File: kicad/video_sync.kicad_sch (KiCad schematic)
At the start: 7 parts, among them J17 Monitor Header, U129 74LS221, U130 74LS221

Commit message: update kicad project
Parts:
- added C87, C88: 1000pF, seequa_footprints:C_Seequa_Bypass_6.5mm, symbol Device:C_Small
- added R11, R80: 6.21 kΩ, seequa_footprints:R_Seequa_Resistor, symbol Device:R_Small
- C105: seq_coord (none) -> L36
- C96, J17: seq_coord (none) -> K33
- R44: seq_coord (none) -> L32; seq_silkscreen R40 -> (none)
- R45: seq_coord (none) -> L33
- U129, U130: seq_coord (none) -> K32; seq_silkscreen (none) -> LS221
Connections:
- net +5V: now also R11.2, R80.2
- net at U129.14 (Cext): now also C87.1
- net at U129.15 (RCext): now also C87.2, R80.1
- net at U129.6 (Cext): now also C88.1
- net at U129.7 (RCext): now also C88.2, R11.1
- net HSYNC_END renamed FRONT_PORCH
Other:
- note added: "Composite HSYNC Pulse"
- note added: "Composite front porch / color burst"

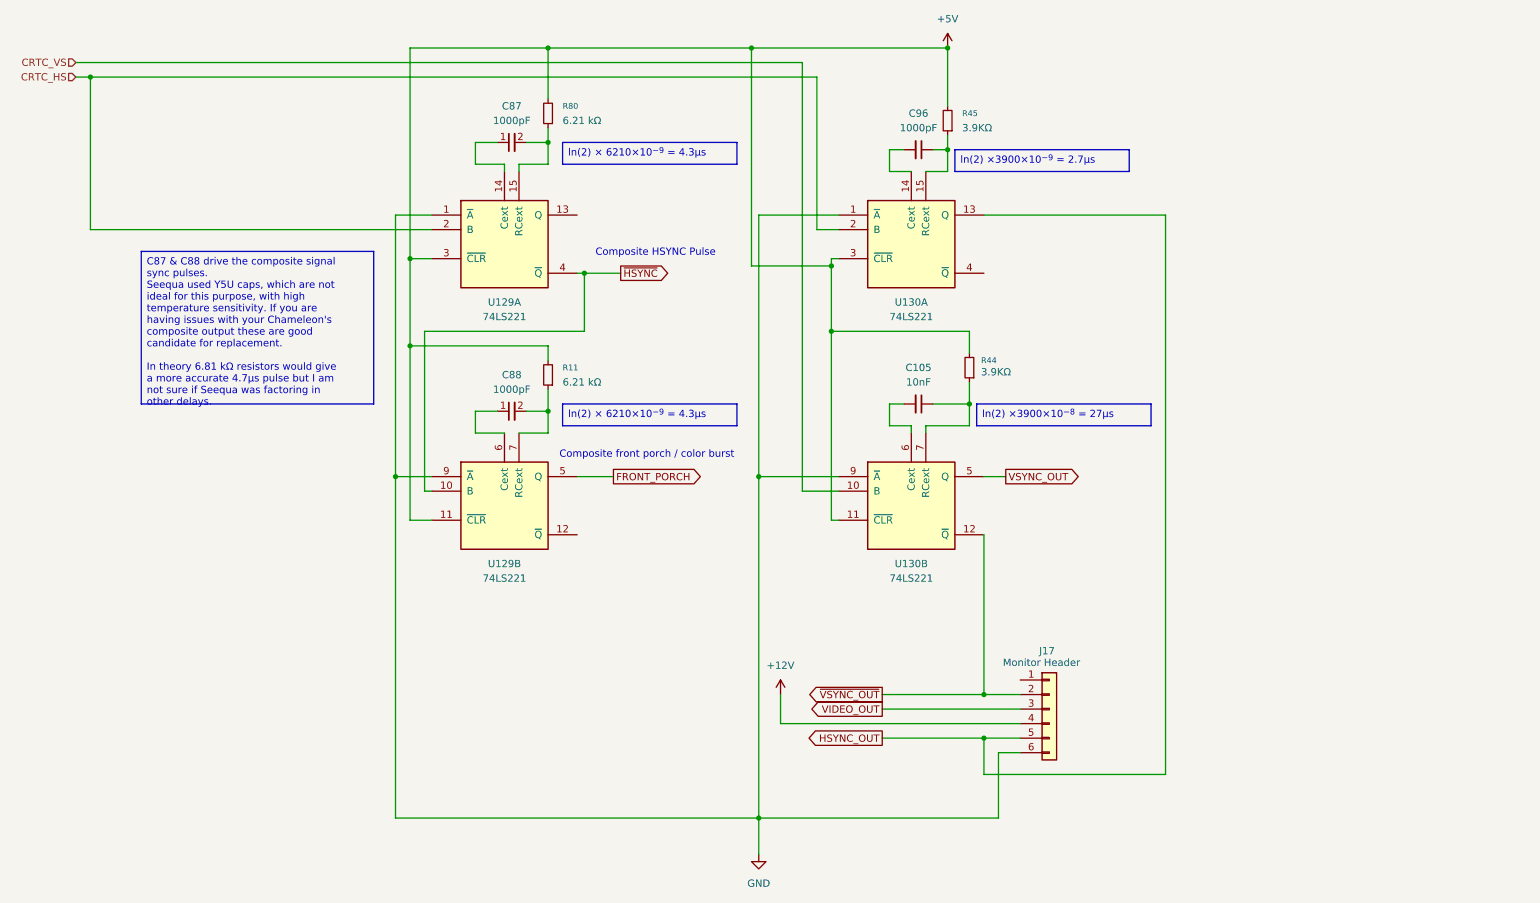
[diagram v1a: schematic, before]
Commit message: Add parallel port, game port
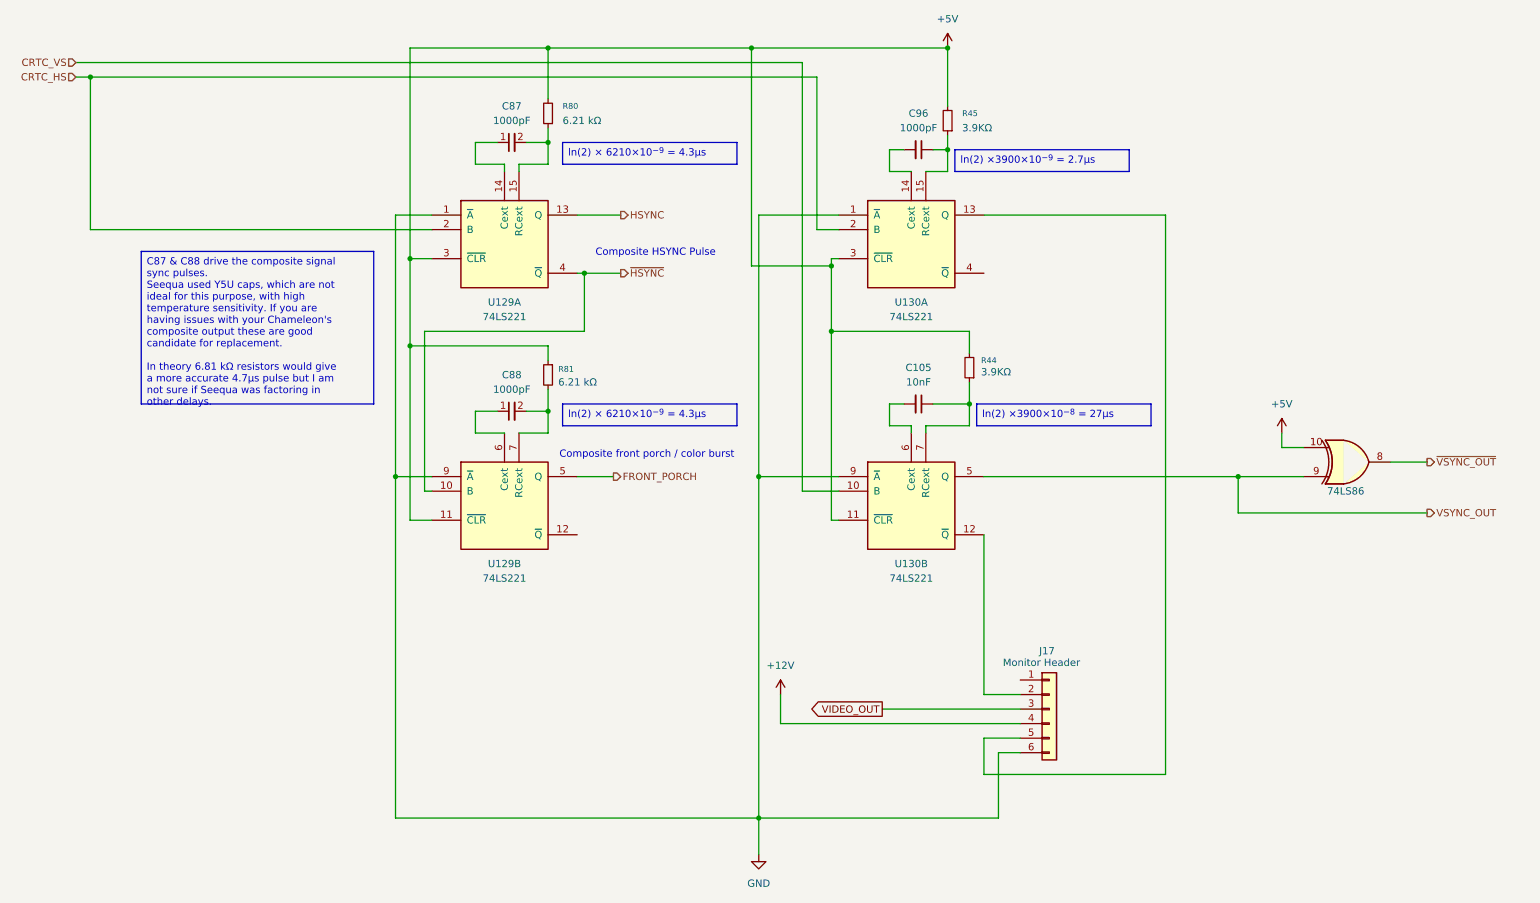
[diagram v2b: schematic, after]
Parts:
- added U139: 74LS86, Package_DIP:DIP-14_W7.62mm, symbol 74xx:74LS86
- renumbered R11 to R81
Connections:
- net +5V: now also R81.1, U139.10; no longer R81.2
- net VSYNC_OUT: now also U139.9
- net ~{VSYNC_OUT}: now also U139.8; no longer J17.2 (Pin_2), U130.12 (~{Q})
- net at C88.2, U129.7 (RCext): now also R81.2; no longer R81.1
- net HSYNC: now reaches U129.13 (Q)
- net HSYNC_OUT: no longer names the net of J17.5 (Pin_5), U130.13 (Q)
- new net: J17.2 (Pin_2), U130.12 (~{Q})
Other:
- moved on the sheet: R81

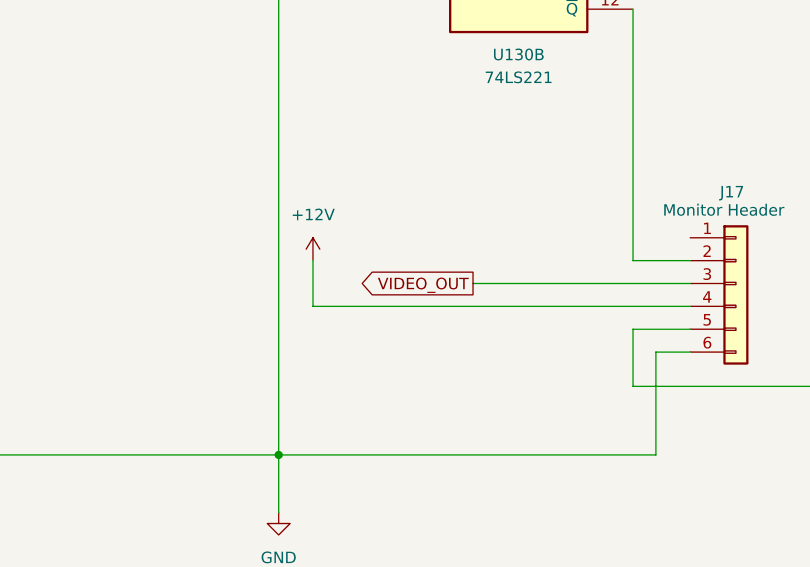
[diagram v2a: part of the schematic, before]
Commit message: A little work on composite output and GPIB
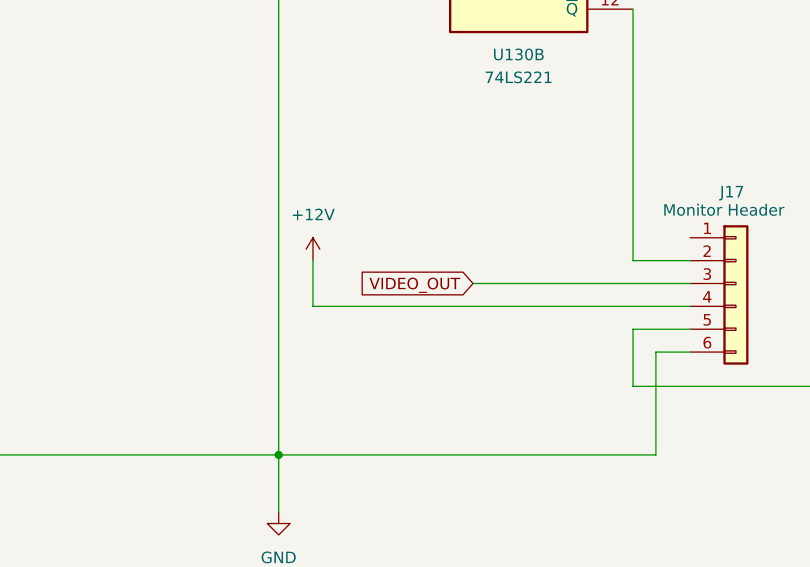
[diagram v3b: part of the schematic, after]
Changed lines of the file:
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@@
 	)
 	(global_label "VIDEO_OUT"
-		(shape output)
+		(shape input)
 		(at 168.91 137.16 180)
 		(fields_autoplaced yes)
